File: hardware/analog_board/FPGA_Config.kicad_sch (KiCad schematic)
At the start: 20 parts, among them J1 2x5 牛角座, U1 GW2A-LV18EQ144, U2 W25Q32JVSS

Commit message: feat: 滤波器&差分转单端电路原理图
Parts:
- U1: footprint ArbWave30_lib:QFP-144_20x20_Pitch0.5mm -> ArbWave30_lib:LQFP-144_20x20_Pitch0.5mm
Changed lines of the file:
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@@
 		(fields_autoplaced yes)
 		(property "Reference" "U1"
-			(at 55.0896 60.96 0)
+			(at 63.9705 60.96 0)
 			(show_name no)
 			(do_not_autoplace no)
@@
 		)
 		(property "Value" "GW2A-LV18EQ144"
-			(at 55.0896 63.5 0)
+			(at 63.9705 63.5 0)
 			(show_name no)
 			(do_not_autoplace no)
@@
 			)
 		)
-		(property "Footprint" "ArbWave30_lib:QFP-144_20x20_Pitch0.5mm"
+		(property "Footprint" "ArbWave30_lib:LQFP-144_20x20_Pitch0.5mm"
 			(at 58.166 59.182 0)
 			(hide yes)

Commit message: feat：模拟板电源 原理图设计
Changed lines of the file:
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@@
 		)
 		(property "Value" "GND"
-			(at 69.85 130.81 0)
-			(show_name no)
-			(do_not_autoplace no)
-			(effects
-				(font
-					(size 1.27 1.27)
-				)
+			(at 72.39 126.9999 0)
+			(show_name no)
+			(do_not_autoplace no)
+			(effects
+				(font
+					(size 1.27 1.27)
+				)
+				(justify left)
 			)
 		)
@@
 		)
 		(property "Value" "GND"
-			(at 218.44 144.78 0)
-			(show_name no)
-			(do_not_autoplace no)
-			(effects
-				(font
-					(size 1.27 1.27)
-				)
+			(at 220.98 140.9699 0)
+			(show_name no)
+			(do_not_autoplace no)
+			(effects
+				(font
+					(size 1.27 1.27)
+				)
+				(justify left)
 			)
 		)
@@
 		)
 		(property "Value" "GND"
-			(at 158.75 54.6099 90)
-			(show_name no)
-			(do_not_autoplace no)
-			(effects
-				(font
-					(size 1.27 1.27)
-				)
-				(justify right)
+			(at 161.29 50.8 90)
+			(show_name no)
+			(do_not_autoplace no)
+			(effects
+				(font
+					(size 1.27 1.27)
+				)
 			)
 		)
@@
 		)
 		(property "Value" "GND"
-			(at 194.31 80.01 0)
-			(show_name no)
-			(do_not_autoplace no)
-			(effects
-				(font
-					(size 1.27 1.27)
-				)
+			(at 196.85 76.1999 0)
+			(show_name no)
+			(do_not_autoplace no)
+			(effects
+				(font
+					(size 1.27 1.27)
+				)
+				(justify left)
 			)
 		)
@@
 		)
 		(property "Value" "+3.3V"
-			(at 168.91 64.7699 90)
-			(show_name no)
-			(do_not_autoplace no)
-			(effects
-				(font
-					(size 1.27 1.27)
-				)
-				(justify left)
+			(at 171.45 62.23 90)
+			(show_name no)
+			(do_not_autoplace no)
+			(effects
+				(font
+					(size 1.27 1.27)
+				)
 			)
 		)
@@
 		(fields_autoplaced yes)
 		(property "Reference" "U1"
-			(at 63.9705 60.96 0)
+			(at 55.0896 60.96 0)
 			(show_name no)
 			(do_not_autoplace no)
@@
 		)
 		(property "Value" "GW2A-LV18EQ144"
-			(at 63.9705 63.5 0)
+			(at 55.0896 63.5 0)
 			(show_name no)
 			(do_not_autoplace no)
@@
 		)
 		(property "Value" "GND"
-			(at 167.64 120.6499 90)
-			(show_name no)
-			(do_not_autoplace no)
-			(effects
-				(font
-					(size 1.27 1.27)
-				)
-				(justify right)
+			(at 170.18 116.84 90)
+			(show_name no)
+			(do_not_autoplace no)
+			(effects
+				(font
+					(size 1.27 1.27)
+				)
 			)
 		)
@@
 		)
 		(property "Value" "+3.3V"
-			(at 194.31 39.37 0)
-			(show_name no)
-			(do_not_autoplace no)
-			(effects
-				(font
-					(size 1.27 1.27)
-				)
-			)
-		)
+			(at 196.85 43.1799 0)
+			(show_name no)
+			(do_not_autoplace no)
+			(effects
+				(font
+					(size 1.27 1.27)
+				)
+				(justify left)
+			)
+		)

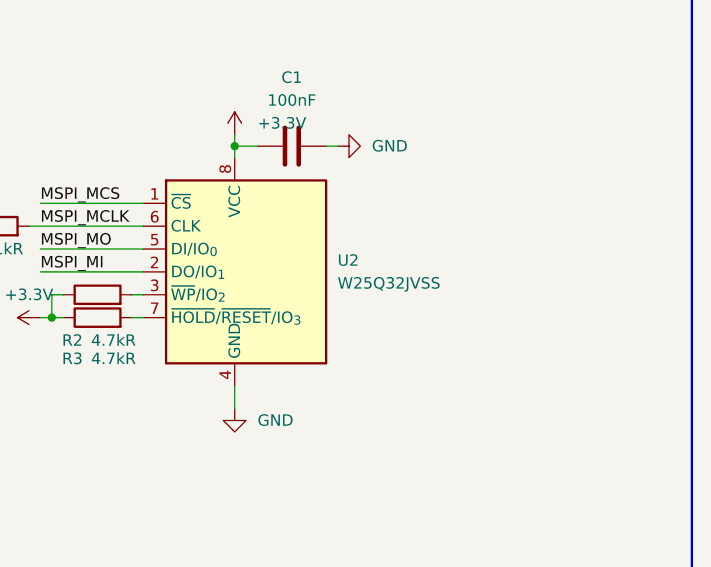
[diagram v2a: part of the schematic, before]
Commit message: feat：DCDC移至控制板
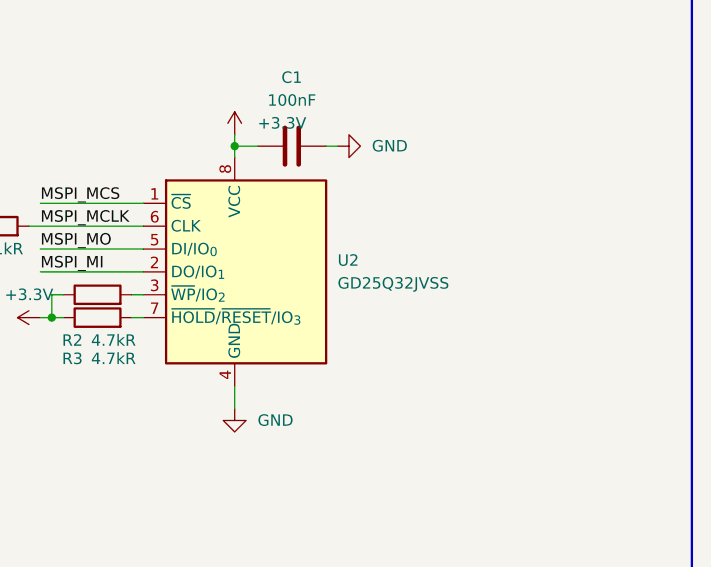
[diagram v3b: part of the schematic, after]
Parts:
- U2: value W25Q32JVSS -> GD25Q32JVSS
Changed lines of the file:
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@@
 			)
 		)
-		(property "Value" "W25Q32JVSS"
+		(property "Value" "GD25Q32JVSS"
 			(at 205.74 60.9599 0)
 			(show_name no)
